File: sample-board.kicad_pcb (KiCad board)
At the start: 2 copper layers, 24 x 17.8 mm, 9 parts, among them J2 USB_B_Micro, U1 LM555xN

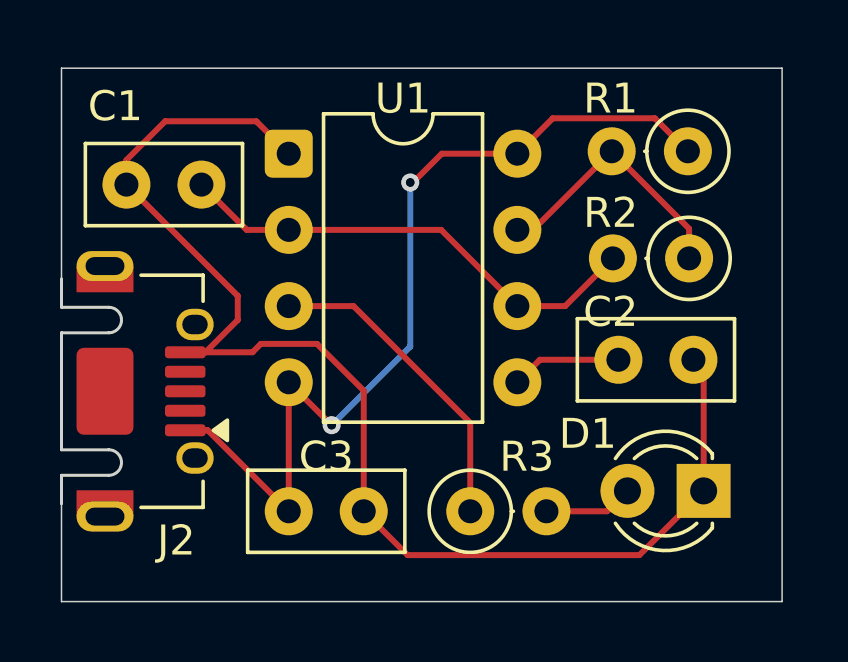
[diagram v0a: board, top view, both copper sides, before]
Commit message: Moving silkscreen again
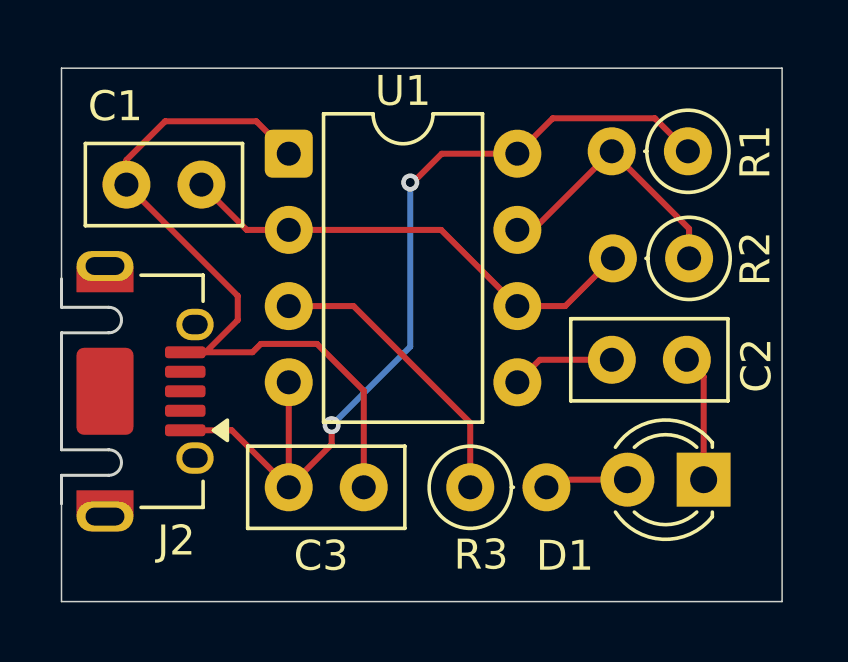
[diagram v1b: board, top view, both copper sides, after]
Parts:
- moved C3 0.80 mm to (149.3, 96.5)
- moved R3 0.80 mm to (155.3, 96.5)
- moved D1 0.37 mm to (163.1, 96.3)
- moved C2 0.22 mm to (160.1, 92.3)
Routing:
- net Net-(D1-K): track 43.5 -> 29.6 mm
- net Net-(U1-OUT): track 10.6 -> 9.81 mm
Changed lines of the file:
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@@
 		(tags "Resistor Axial_DIN0207 series Axial Vertical pin pitch 2.54mm 0.25W = 1/4W length 6.3mm diameter 2.5mm")
 		(property "Reference" "R1"
-			(at 2.575 1.754 0)
+			(at -2.251 -0.024 90)
 			(layer "F.SilkS")
 			(effects
@@
 		)
 		(fp_text user "${REFERENCE}"
-			(at 1.27 -2.37 0)
+			(at 1.813 -1.802 0)
 			(layer "F.Fab")
 			(effects
@@
 		(tags "THT DIP DIL PDIP 2.54mm 7.62mm 300mil")
 		(property "Reference" "U1"
-			(at 3.81 -1.834 0)
+			(at 3.81 -2.088 0)
 			(layer "F.SilkS")
 			(effects
@@
 	(footprint "Capacitor_THT:C_Disc_D5.0mm_W2.5mm_P2.50mm"
 		(layer "F.Cu")
-		(at 149.29 97.32)
+		(at 149.29 96.52)
 		(descr "C, Disc series, Radial, pin pitch=2.50mm, diameter*width=5*2.5mm^2, Capacitor, http://cdn-reichelt.de/documents/datenblatt/B300/DS_KERKO_TC.pdf")
 		(tags "C Disc series Radial pin pitch 2.50mm diameter 5mm width 2.5mm Capacitor")
 		(property "Reference" "C3"
-			(at 1.25 -1.816 0)
+			(at 1.078 2.286 0)
 			(layer "F.SilkS")
 			(effects
@@
 		(tags "Resistor Axial_DIN0207 series Axial Vertical pin pitch 2.54mm 0.25W = 1/4W length 6.3mm diameter 2.5mm")
 		(property "Reference" "R2"
-			(at 2.615 1.514 0)
+			(at -2.211 -0.01 270)
 			(layer "F.SilkS")
 			(effects
@@
 	(footprint "Resistor_THT:R_Axial_DIN0207_L6.3mm_D2.5mm_P2.54mm_Vertical"
 		(layer "F.Cu")
-		(at 155.34 97.32)
+		(at 155.34 96.52)
 		(descr "Resistor, Axial_DIN0207 series, Axial, Vertical, pin pitch=2.54mm, 0.25W = 1/4W, length*diameter=6.3*2.5mm^2, http://cdn-reichelt.de/documents/datenblatt/B400/1_4W%23YAG.pdf")
 		(tags "Resistor Axial_DIN0207 series Axial Vertical pin pitch 2.54mm 0.25W = 1/4W length 6.3mm diameter 2.5mm")
 		(property "Reference" "R3"
-			(at 1.886 -1.816 0)
+			(at 0.362 2.248 0)
 			(layer "F.SilkS")
 			(effects
@@
 	(footprint "LED_THT:LED_D3.0mm"
 		(layer "F.Cu")
-		(at 163.12 96.64 180)
+		(at 163.12 96.266 180)
 		(descr "LED, diameter 3.0mm, 2 pins, generated by kicad-footprint-generator")
 		(tags "LED")
 		(property "Reference" "D1"
-			(at 3.862 1.898 0)
+			(at 4.624 -2.54 0)
 			(layer "F.SilkS")
 			(effects
@@
 		)
 		(point
-			(at 161.85 96.64)
+			(at 161.85 96.266)
 			(size 2)
 			(layer "F.Fab")
@@
 	(footprint "Capacitor_THT:C_Disc_D5.0mm_W2.5mm_P2.50mm"
 		(layer "F.Cu")
-		(at 160.28 92.27)
+		(at 160.06 92.27)
 		(descr "C, Disc series, Radial, pin pitch=2.50mm, diameter*width=5*2.5mm^2, Capacitor, http://cdn-reichelt.de/documents/datenblatt/B300/DS_KERKO_TC.pdf")
 		(tags "C Disc series Radial pin pitch 2.50mm diameter 5mm width 2.5mm Capacitor")
 		(property "Reference" "C2"
-			(at -0.26 -1.592 0)
+			(at 4.82 0.186 90)
 			(layer "F.SilkS")
 			(effects
@@
 	)
 	(segment
+		(start 149.29 96.52)
+		(end 149.29 93.02)
+		(width 0.2)
+		(layer "F.Cu")
+		(net "Net-(J2-VBUS)")
+	)
+	(segment
 		(start 161.495 84.22)
 		(end 162.595 85.32)
@@
 	)
 	(segment
-		(start 149.29 93.02)
-		(end 149.29 97.32)
+		(start 149.29 96.52)
+		(end 147.39 94.62)
+		(width 0.2)
+		(layer "F.Cu")
+		(net "Net-(J2-VBUS)")
+	)
+	(segment
+		(start 147.39 94.62)
+		(end 145.84 94.62)
 		(width 0.2)
 		(layer "F.Cu")
@@
 	)
 	(segment
-		(start 149.29 93.02)
-		(end 150.72 94.45)
+		(start 150.72 94.45)
+		(end 150.72 95.09)
 		(width 0.2)
 		(layer "F.Cu")
@@
 	)
 	(segment
-		(start 145.84 94.62)
-		(end 146.59 94.62)
-		(width 0.2)
-		(layer "F.Cu")
-		(net "Net-(J2-VBUS)")
-	)
-	(segment
-		(start 146.59 94.62)
-		(end 149.29 97.32)
+		(start 150.72 95.09)
+		(end 149.29 96.52)
 		(width 0.2)
 		(layer "F.Cu")
@@
 	)
 	(segment
-		(start 153.25 98.78)
-		(end 160.98 98.78)
+		(start 163.12 92.83)
+		(end 163.12 96.266)
 		(width 0.2)
 		(layer "F.Cu")
@@
 	)
 	(segment
-		(start 151.79 93.3)
-		(end 151.79 97.32)
-		(width 0.2)
-		(layer "F.Cu")
-		(net "Net-(D1-K)")
-	)
-	(segment
-		(start 151.79 97.32)
-		(end 153.25 98.78)
+		(start 162.56 92.27)
+		(end 163.12 92.83)
 		(width 0.2)
 		(layer "F.Cu")
@@
 	)
 	(segment
-		(start 163.12 92.61)
-		(end 162.78 92.27)
-		(width 0.2)
-		(layer "F.Cu")
-		(net "Net-(D1-K)")
-	)
-	(segment
 		(start 148.21 84.32)
 		(end 145.17 84.32)
@@
 	)
 	(segment
-		(start 163.12 96.64)
-		(end 163.12 92.61)
-		(width 0.2)
-		(layer "F.Cu")
-		(net "Net-(D1-K)")
-	)
-	(segment
 		(start 146.514999 92.02)
 		(end 145.84 92.02)
@@
 	)
 	(segment
+		(start 151.79 96.52)
+		(end 151.79 93.3)
+		(width 0.2)
+		(layer "F.Cu")
+		(net "Net-(D1-K)")
+	)
+	(segment
 		(start 143.88 85.61)
 		(end 143.88 86.43)
@@
 	)
 	(segment
-		(start 160.98 98.78)
-		(end 163.12 96.64)
-		(width 0.2)
-		(layer "F.Cu")
-		(net "Net-(D1-K)")
-	)
-	(segment
 		(start 148.36 91.74)
 		(end 150.23 91.74)
@@
 	)
 	(segment
-		(start 155.34 97.32)
-		(end 155.34 94.37)
-		(width 0.2)
-		(layer "F.Cu")
-		(net "Net-(U1-OUT)")
-	)
-	(segment
 		(start 155.34 94.37)
 		(end 151.45 90.48)
@@
 	)
 	(segment
-		(start 157.88 97.32)
-		(end 159.9 97.32)
+		(start 155.34 96.52)
+		(end 155.34 94.37)
+		(width 0.2)
+		(layer "F.Cu")
+		(net "Net-(U1-OUT)")
+	)
+	(segment
+		(start 158.134 96.266)
+		(end 157.88 96.52)
 		(width 0.2)
 		(layer "F.Cu")
@@
 	)
 	(segment
-		(start 159.9 97.32)
-		(end 160.58 96.64)
-		(width 0.2)
-		(layer "F.Cu")
+		(start 160.58 96.266)
+		(end 158.134 96.266)
+		(width 0.2)
+		(layer "F.Cu")

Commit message: Adding missing trace
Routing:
- net Net-(D1-K): track 29.6 -> 42.0 mm
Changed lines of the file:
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@@
+	)
+	(segment
+		(start 152.89 97.62)
+		(end 161.766 97.62)
+		(width 0.2)
+		(layer "F.Cu")
+		(net "Net-(D1-K)")
 	)
 	(segment
@@
 	)
 	(segment
+		(start 151.79 96.52)
+		(end 152.89 97.62)
+		(width 0.2)
+		(layer "F.Cu")
+		(net "Net-(D1-K)")
+	)
+	(segment
 		(start 147.59 90.14)
 		(end 147.59 90.944999)
@@
 		(width 0.2)
 		(layer "F.Cu")
+		(net "Net-(D1-K)")
+	)
+	(segment
+		(start 161.766 97.62)
+		(end 163.12 96.266)
+		(width 0.2)
+		(layer "F.Cu")
